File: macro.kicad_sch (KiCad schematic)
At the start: 52 parts, among them J1 Conn_01x01_Male, J2 Conn_01x01_Male, J3 Conn_01x01_Male, SW1 SW_Push, SW2 RotaryEncoder_Switch, SW3 SW_Push, U1 RP2040, U2 AP2112K-3.3, U3 W25Q128JVPIQ, Y1 12MHz

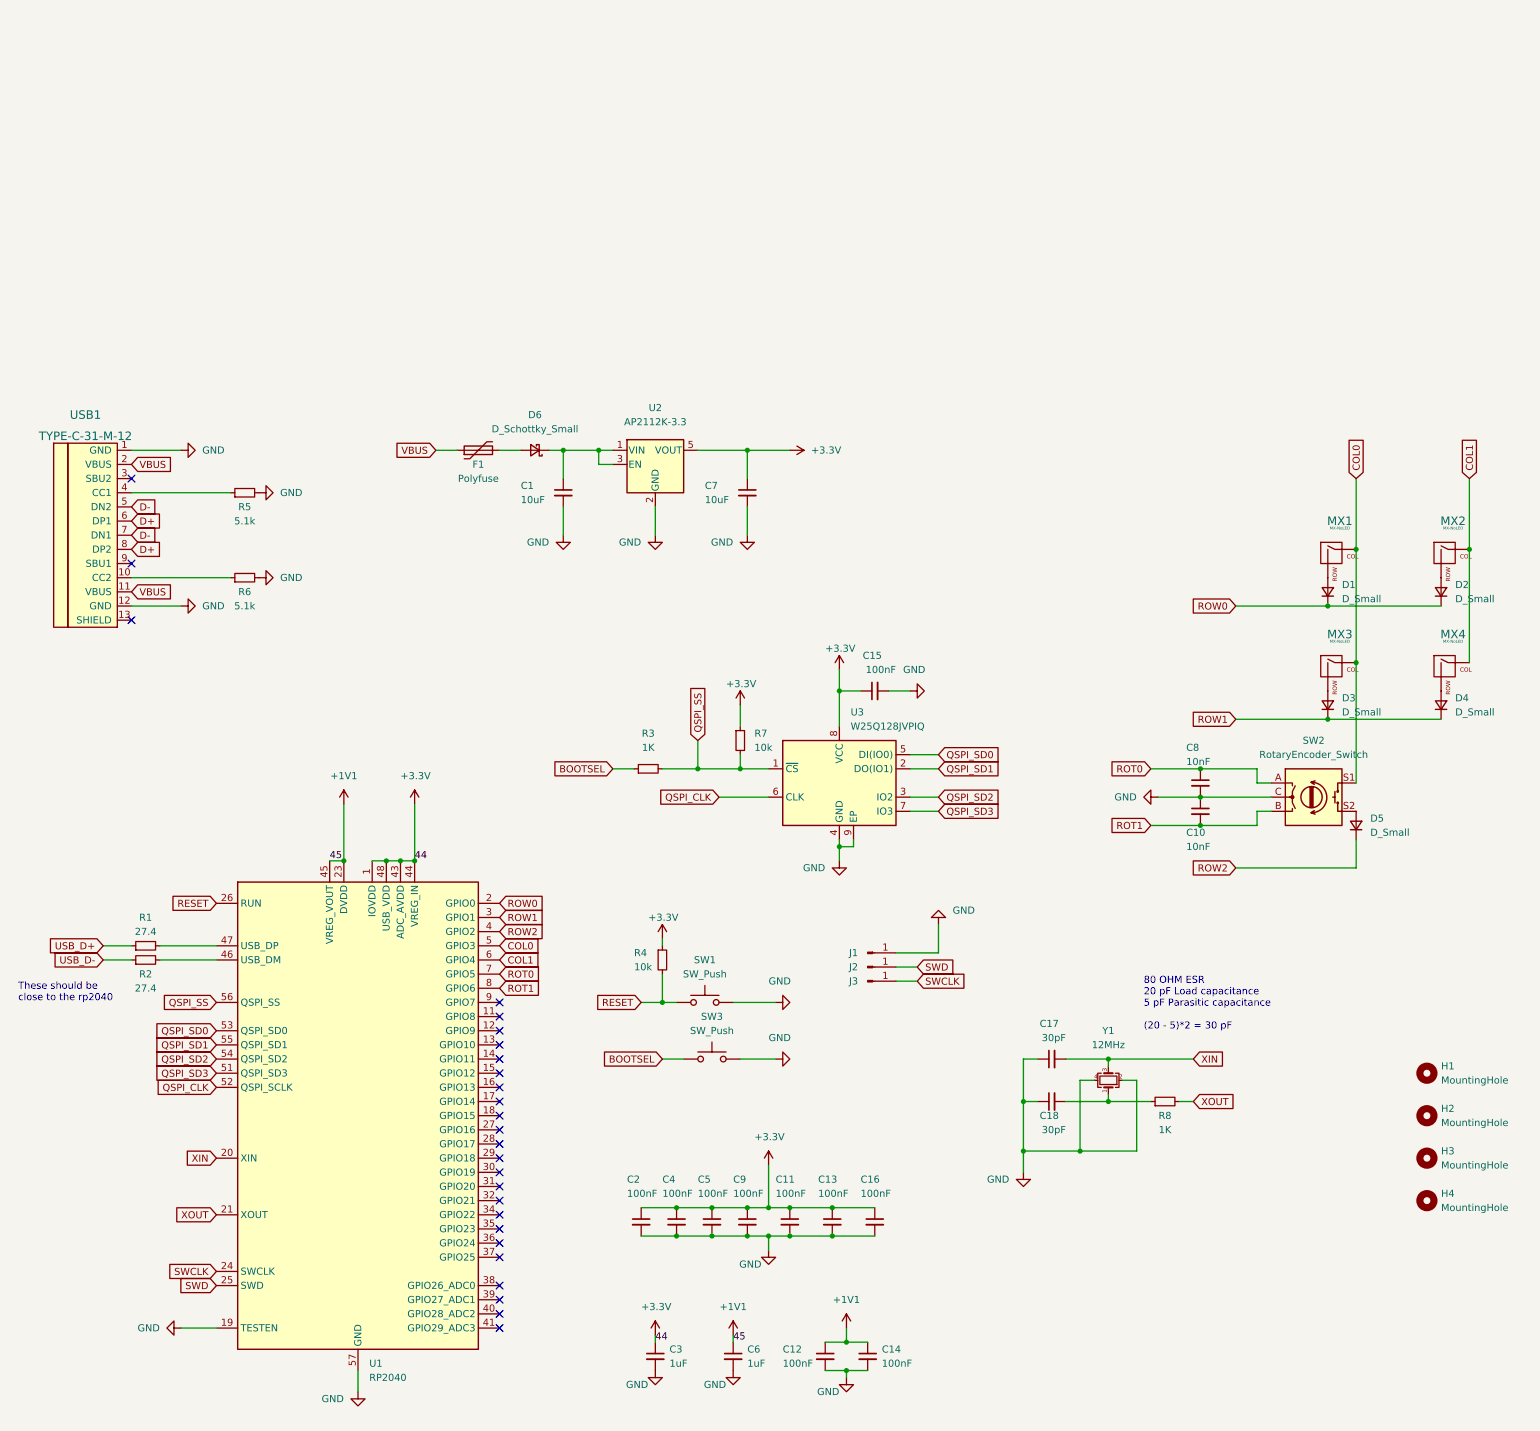
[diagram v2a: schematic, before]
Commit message: Rough placement
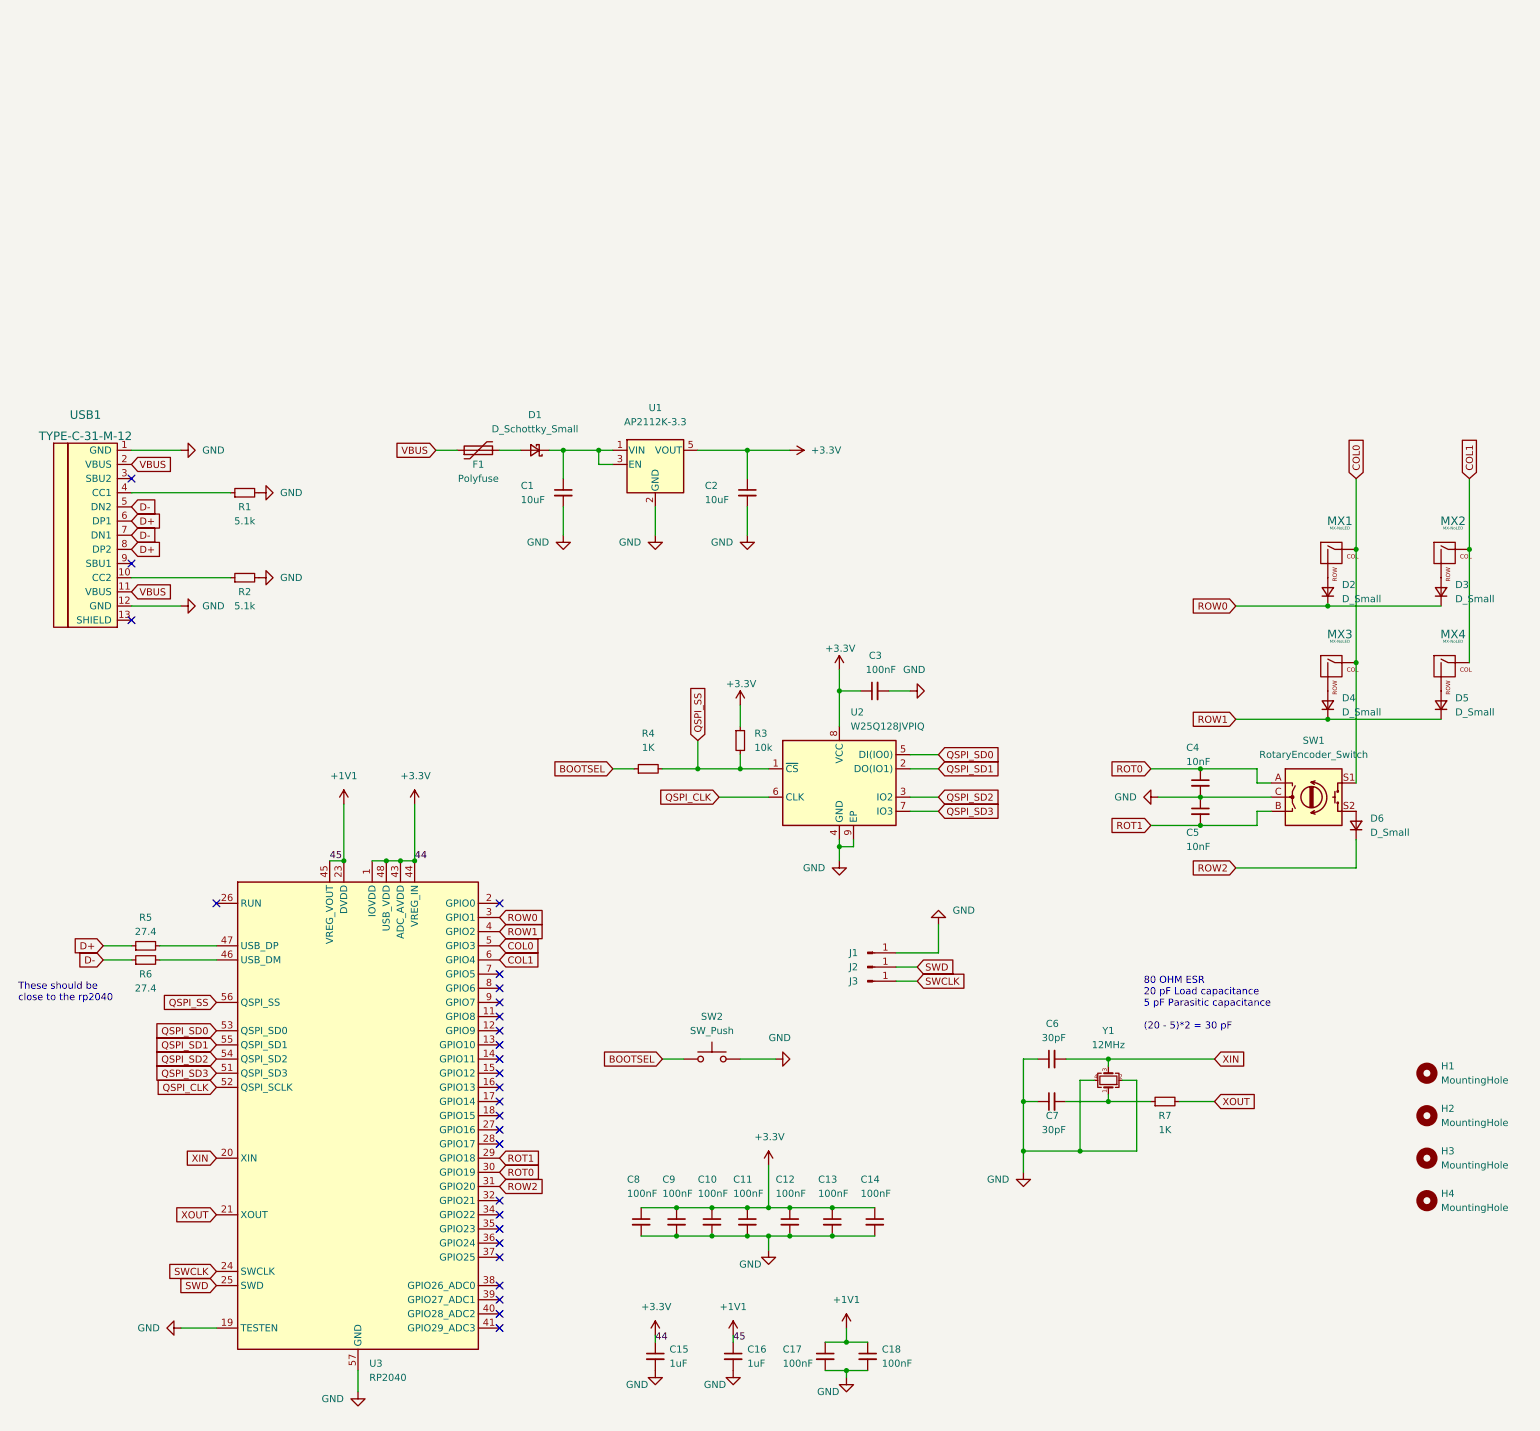
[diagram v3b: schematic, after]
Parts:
- removed R4: 10k, Resistor_SMD:R_0402_1005Metric, symbol Device:R_Small
- removed SW1: SW_Push, Button_Switch_SMD:SW_Push_1P1T_NO_CK_KMR2, symbol Switch:SW_Push
- renumbered C5 to C10, C9 to C11, C11 to C12, C16 to C14, C3 to C15, C6 to C16, C12 to C17, C14 to C18, C7 to C2, C15 to C3, C8 to C4, C10 to C5, C17 to C6, C18 to C7, C2 to C8, C4 to C9, D6 to D1, D1 to D2, D2 to D3, D3 to D4, D4 to D5, D5 to D6, R5 to R1, R6 to R2, R7 to R3, R3 to R4, R1 to R5, R2 to R6, R8 to R7, SW2 to SW1, SW3 to SW2, U2 to U1, U3 to U2, U1 to U3
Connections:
- net USB_D+ is gone; now on net D+: R5.1
- net USB_D- is gone; now on net D-: R6.1
- net ROT0: now also U3.30 (GPIO19); no longer U3.7 (GPIO5)
- net ROT1: now also U3.29 (GPIO18); no longer U3.8 (GPIO6)
- net ROW0: now also U3.3 (GPIO1); no longer U3.2 (GPIO0)
- net ROW1: now also U3.4 (GPIO2); no longer U3.3 (GPIO1)
- net ROW2: now also U3.31 (GPIO20); no longer U3.4 (GPIO2)
- net RESET: no longer names the net of U3.26 (RUN)
- no-connect marks 26 -> 27

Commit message: v0
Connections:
- net COL0: now also U3.6 (GPIO4); no longer U3.5 (GPIO3)
- net COL1: now also U3.4 (GPIO2); no longer U3.6 (GPIO4)
- net D+: now also R5.2, U3.47 (USB_DP)
- net D-: now also R6.2, U3.46 (USB_DM)
- net ROW1: now also U3.5 (GPIO3); no longer U3.4 (GPIO2)
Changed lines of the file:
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@@
+    (effects (font (size 1.27 1.27)) (justify left bottom))
+  )
+  (label "D-" (at 41.91 115.57 0)
     (effects (font (size 1.27 1.27)) (justify left bottom))
   )
   (label "44" (at 128.27 184.15 0)
+    (effects (font (size 1.27 1.27)) (justify left bottom))
+  )
+  (label "D+" (at 41.91 113.03 0)
     (effects (font (size 1.27 1.27)) (justify left bottom))
   )
@@
     )
   )
-  (global_label "ROW1" (shape input) (at 100.33 110.49 0) (fields_autoplaced)
+  (global_label "ROW1" (shape input) (at 100.33 113.03 0) (fields_autoplaced)
     (effects (font (size 1.27 1.27)) (justify left))
-    (property "Intersheet References" "${INTERSHEET_REFS}" (id 0) (at 108.0045 110.4106 0)
+    (property "Intersheet References" "${INTERSHEET_REFS}" (id 0) (at 108.0045 112.9506 0)
       (effects (font (size 1.27 1.27)) (justify left) hide)
     )
@@
     )
   )
-  (global_label "COL1" (shape input) (at 100.33 115.57 0) (fields_autoplaced)
+  (global_label "COL1" (shape input) (at 100.33 110.49 0) (fields_autoplaced)
     (effects (font (size 1.27 1.27)) (justify left))
-    (property "Intersheet References" "${INTERSHEET_REFS}" (id 0) (at 107.5812 115.4906 0)
+    (property "Intersheet References" "${INTERSHEET_REFS}" (id 0) (at 107.5812 110.4106 0)
       (effects (font (size 1.27 1.27)) (justify left) hide)
     )
@@
     )
   )
-  (global_label "COL0" (shape input) (at 100.33 113.03 0) (fields_autoplaced)
+  (global_label "COL0" (shape input) (at 100.33 115.57 0) (fields_autoplaced)
     (effects (font (size 1.27 1.27)) (justify left))
-    (property "Intersheet References" "${INTERSHEET_REFS}" (id 0) (at 107.5812 112.9506 0)
+    (property "Intersheet References" "${INTERSHEET_REFS}" (id 0) (at 107.5812 115.4906 0)
       (effects (font (size 1.27 1.27)) (justify left) hide)
     )

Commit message: LEDs
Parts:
- added D10, D11, D12, D7, D8, D9: WS2812B, LED_SMD:LED_WS2812B-2020_PLCC4_2.0x2.0mm, symbol LED:WS2812B
- added Q1: BSS138, Package_TO_SOT_SMD:SOT-23, symbol Transistor_FET:BSS138
- added R10, R8, R9: 10k, Resistor_SMD:R_0402_1005Metric, symbol Device:R_Small
- added TP1, TP2: TestPoint, TestPoint:TestPoint_Pad_D1.0mm, symbol Connector:TestPoint
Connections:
- net +3.3V: now also Q1.1 (G), R8.1, TP2.1
- net GND: now also D10.1 (VDD), D11.1 (VDD), D12.1 (VDD), D7.1 (VDD), D8.1 (VDD), D9.1 (VDD)
- net +5V: now reaches C1.1, D1.1 (K), U1.1 (VIN)
- net +5V: now also D10.3 (VSS), D11.3 (VSS), D12.3 (VSS), D7.3 (VSS), D8.3 (VSS), D9.3 (VSS), R10.1, R9.1, TP1.1; no longer U1.3 (EN)
- net LED_DIN: now reaches U3.32 (GPIO21)
- net LED_DIN: now also Q1.2 (S), R8.2
- new net: D7.2 (DOUT), D8.4 (DIN)
- new net: D7.4 (DIN), Q1.3 (D), R9.2
- new net: D11.4 (DIN), D12.2 (DOUT)
- new net: D12.4 (DIN), D9.2 (DOUT)
- new net: D8.2 (DOUT), D9.4 (DIN)
- new net: D10.4 (DIN), D11.2 (DOUT)
- new net: R10.2, U1.3 (EN)
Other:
- note added: "80 ohm ESR 20 pF Load capacitance 5 pF Parasitic capacitance (20 - 5)*2 = 30 pF"
- note removed: "80 OHM ESR 20 pF Load capacitance 5 pF Parasitic capacitance (20 - 5)*2 = 30 pF"
- moved on the sheet: C1, C2, D1, F1, U1

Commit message: Cleanup schematic
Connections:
- net +5V: now also D10.1 (VDD), D11.1 (VDD), D12.1 (VDD), D7.1 (VDD), D8.1 (VDD), D9.1 (VDD); no longer D10.3 (VSS), D11.3 (VSS), D12.3 (VSS), D7.3 (VSS), D8.3 (VSS), D9.3 (VSS)
- net GND: now also D10.3 (VSS), D11.3 (VSS), D12.3 (VSS), D7.3 (VSS), D8.3 (VSS), D9.3 (VSS); no longer D10.1 (VDD), D11.1 (VDD), D12.1 (VDD), D7.1 (VDD), D8.1 (VDD), D9.1 (VDD)
- net LED_DIN_5V: now reaches D7.4 (DIN), Q1.3 (D), R9.2
- net LED_DIN renamed LED_DIN_3V3
- net XIN: no longer names the net of C6.2, U3.20 (XIN), Y1.3
- net XOUT: no longer names the net of R7.2, U3.21 (XOUT)
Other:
- note added: "LED Signal Level Shifter"
- note added: "MCU"
- note added: "POWER"
- note added: "QSPI FLASH"
- note added: "SWD Pads"
- note added: "USB"
- moved on the sheet: C1, C10, C11, C12, C13, C14, C15, C16, C17, C18, C2, C3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

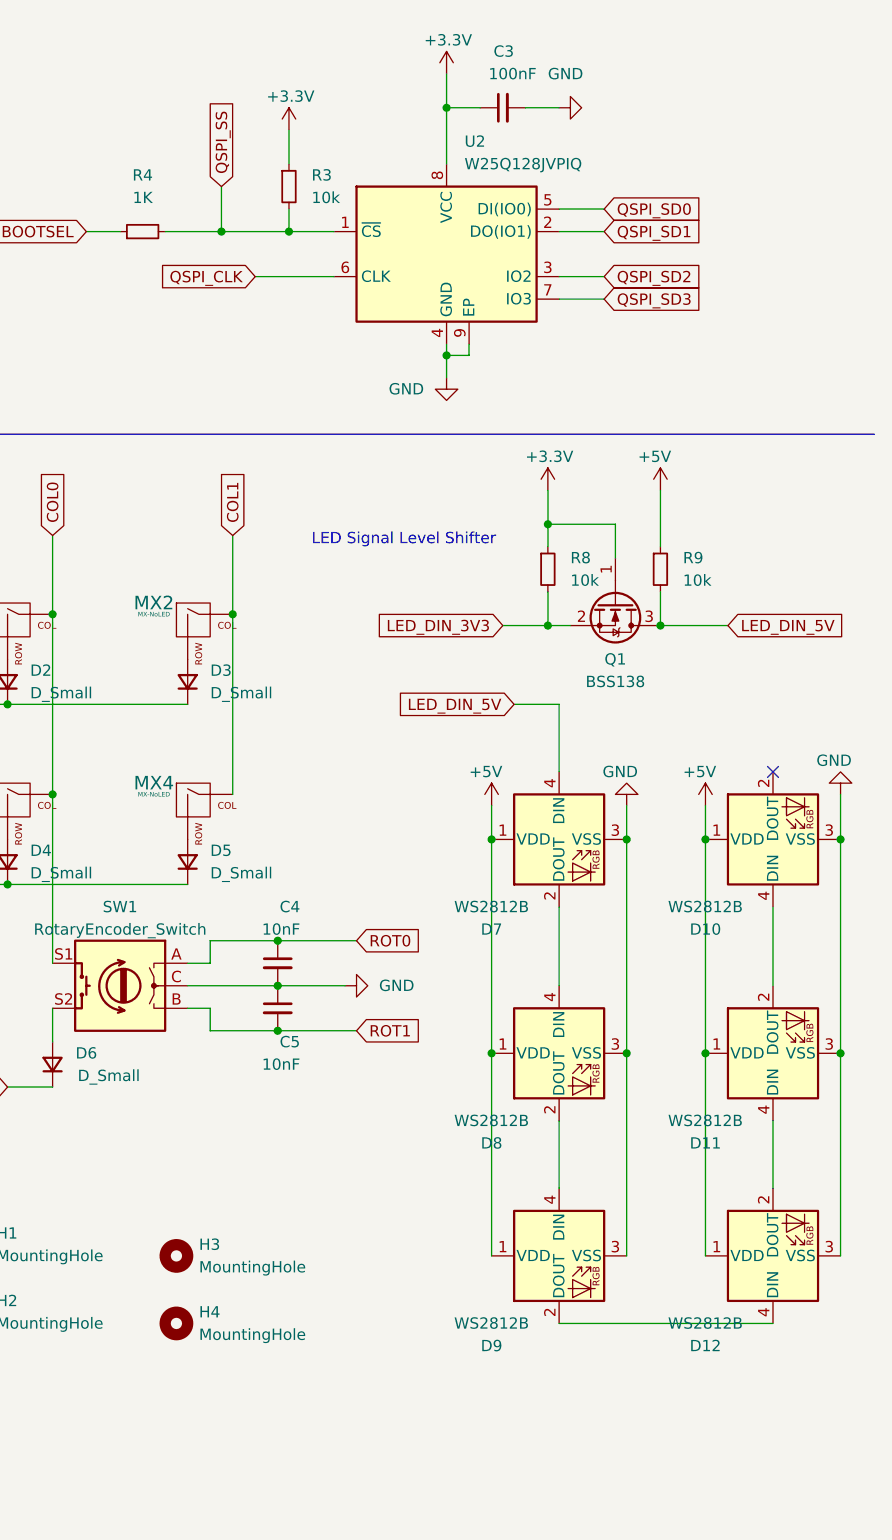
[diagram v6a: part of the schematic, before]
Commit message: Add LED decoupling caps
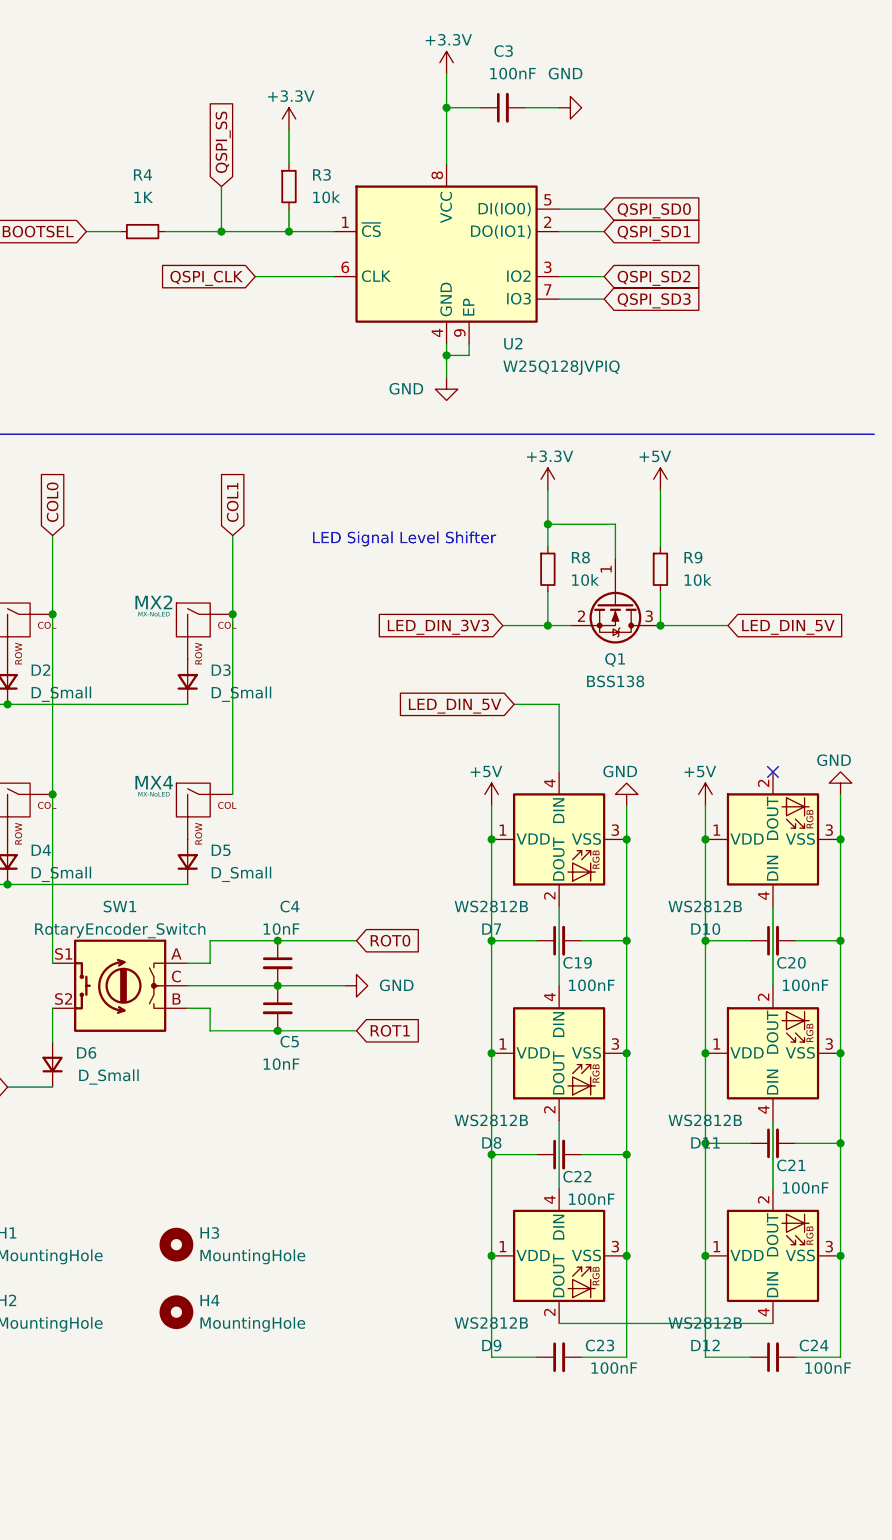
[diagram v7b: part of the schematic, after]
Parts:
- added C19, C20, C21, C22, C23, C24: 100nF, Capacitor_SMD:C_0402_1005Metric, symbol Device:C_Small
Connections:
- net +5V: now also C19.1, C20.1, C21.1, C22.1, C23.1, C24.1
- net GND: now also C19.2, C20.2, C21.2, C22.2, C23.2, C24.2
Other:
- moved on the sheet: H3, H4

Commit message: Update
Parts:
- removed C19, C20, C21, C22, C23, C24: 100nF, Capacitor_SMD:C_0402_1005Metric, symbol Device:C_Small
